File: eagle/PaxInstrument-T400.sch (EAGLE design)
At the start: 115 parts, among them IC1 MCP3424, J1 MICRO-SDCARD-CONNECTOR-330006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, U1 MCP9800, U3 MCP73831, U4 MIC5219-3.3V, U8 NC7S32, X1 FH12-12S-0.5SH, Y1 RESONATORSMD

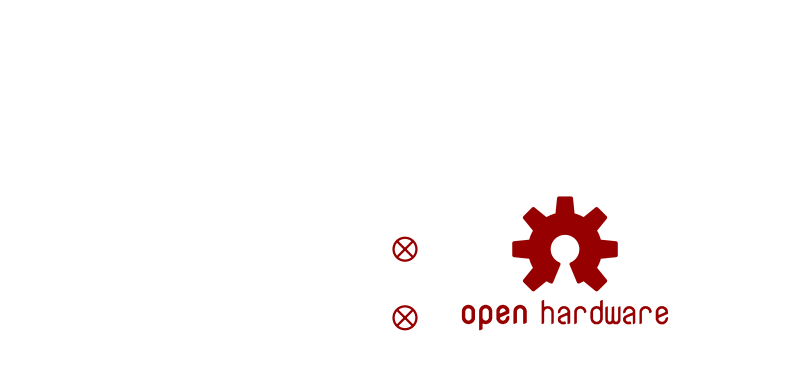
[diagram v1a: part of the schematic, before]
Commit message: Remove fiducials for Rev 0.10
Fix issue Remove fiducials #125
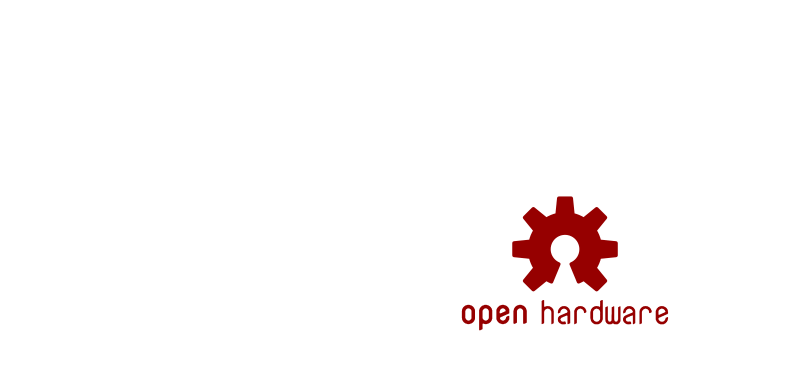
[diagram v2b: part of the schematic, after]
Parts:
- removed FID1, FID2: FIDUCIAL1X2, SparkFun-Aesthetics:FIDUCIAL1X2
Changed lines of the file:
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@@
 <attribute name="OC_DIGIKEY" value="1276-5086-2-ND"/>
-</part>
-<part name="FID1" library="SparkFun-Aesthetics" deviceset="FIDUCIAL" device="1X2">
-<attribute name="MPN" value="N/A"/>
-<attribute name="OC_DIGIKEY" value="N/A"/>
-</part>
-<part name="FID2" library="SparkFun-Aesthetics" deviceset="FIDUCIAL" device="1X2">
-<attribute name="MPN" value="N/A"/>
-<attribute name="OC_DIGIKEY" value="N/A"/>
 </part>
 <part name="U$1" library="blinkinlabs" deviceset="USB_MICRO" device="SMT+THRUHULE">
@@
 <attribute name="MPN" x="124.46" y="200.66" size="1.778" layer="96" display="off"/>
 </instance>
-<instance part="FID1" gate="G$1" x="254" y="15.24">
-<attribute name="MPN" x="254" y="15.24" size="1.778" layer="96" display="off"/>
-<attribute name="OC_DIGIKEY" x="254" y="15.24" size="1.778" layer="96" display="off"/>
-</instance>
-<instance part="FID2" gate="G$1" x="254" y="7.62">
-<attribute name="MPN" x="254" y="7.62" size="1.778" layer="96" display="off"/>
-<attribute name="OC_DIGIKEY" x="254" y="7.62" size="1.778" layer="96" display="off"/>
-</instance>
 <instance part="U$1" gate="G$1" x="17.78" y="233.68">

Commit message: Changed Longer soler pads on 2x3 header footprint for Rev 0.10
Changed Longer soler pads on 2x3 header footprint #122
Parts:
- ICSP, ICSP1: device SparkFun-Connectors:M03X2SMT -> PaxInstrument-T400:SPARKFUN-CONNECTORS_M03X2PAX
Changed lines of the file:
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@@
 <grid distance="0.1" unitdist="inch" unit="inch" style="lines" multiple="1" display="no" altdistance="0.01" altunitdist="inch" altunit="inch"/>
 <layers>
-<layer number="1" name="Top" color="4" fill="1" visible="no" active="no"/>
-<layer number="2" name="Route2" color="1" fill="3" visible="no" active="no"/>
-<layer number="3" name="Route3" color="4" fill="3" visible="no" active="no"/>
-<layer number="4" name="Route4" color="1" fill="4" visible="no" active="no"/>
-<layer number="5" name="Route5" color="4" fill="4" visible="no" active="no"/>
-<layer number="6" name="Route6" color="1" fill="8" visible="no" active="no"/>
-<layer number="7" name="Route7" color="4" fill="8" visible="no" active="no"/>
-<layer number="8" name="Route8" color="1" fill="2" visible="no" active="no"/>
-<layer number="9" name="Route9" color="4" fill="2" visible="no" active="no"/>
-<layer number="10" name="Route10" color="1" fill="7" visible="no" active="no"/>
-<layer number="11" name="Route11" color="4" fill="7" visible="no" active="no"/>
-<layer number="12" name="Route12" color="1" fill="5" visible="no" active="no"/>
-<layer number="13" name="Route13" color="4" fill="5" visible="no" active="no"/>
-<layer number="14" name="Route14" color="1" fill="6" visible="no" active="no"/>
-<layer number="15" name="Route15" color="4" fill="6" visible="no" active="no"/>
-<layer number="16" name="Bottom" color="1" fill="1" visible="no" active="no"/>
-<layer number="17" name="Pads" color="2" fill="1" visible="no" active="no"/>
-<layer number="18" name="Vias" color="2" fill="1" visible="no" active="no"/>
-<layer number="19" name="Unrouted" color="6" fill="1" visible="no" active="no"/>
-<layer number="20" name="Dimension" color="13" fill="1" visible="no" active="no"/>
-<layer number="21" name="tPlace" color="7" fill="1" visible="no" active="no"/>
-<layer number="22" name="bPlace" color="14" fill="1" visible="no" active="no"/>
-<layer number="23" name="tOrigins" color="15" fill="1" visible="no" active="no"/>
-<layer number="24" name="bOrigins" color="15" fill="1" visible="no" active="no"/>
-<layer number="25" name="tNames" color="7" fill="1" visible="no" active="no"/>
-<layer number="26" name="bNames" color="7" fill="1" visible="no" active="no"/>
-<layer number="27" name="tValues" color="7" fill="1" visible="no" active="no"/>
-<layer number="28" name="bValues" color="7" fill="1" visible="no" active="no"/>
+<layer number="1" name="Top" color="4" fill="1" visible="yes" active="no"/>
+<layer number="2" name="Route2" color="1" fill="3" visible="yes" active="no"/>
+<layer number="3" name="Route3" color="4" fill="3" visible="yes" active="no"/>
+<layer number="4" name="Route4" color="1" fill="4" visible="yes" active="no"/>
+<layer number="5" name="Route5" color="4" fill="4" visible="yes" active="no"/>
+<layer number="6" name="Route6" color="1" fill="8" visible="yes" active="no"/>
+<layer number="7" name="Route7" color="4" fill="8" visible="yes" active="no"/>
+<layer number="8" name="Route8" color="1" fill="2" visible="yes" active="no"/>
+<layer number="9" name="Route9" color="4" fill="2" visible="yes" active="no"/>
+<layer number="10" name="Route10" color="1" fill="7" visible="yes" active="no"/>
+<layer number="11" name="Route11" color="4" fill="7" visible="yes" active="no"/>
+<layer number="12" name="Route12" color="1" fill="5" visible="yes" active="no"/>
+<layer number="13" name="Route13" color="4" fill="5" visible="yes" active="no"/>
+<layer number="14" name="Route14" color="1" fill="6" visible="yes" active="no"/>
+<layer number="15" name="Route15" color="4" fill="6" visible="yes" active="no"/>
+<layer number="16" name="Bottom" color="1" fill="1" visible="yes" active="no"/>
+<layer number="17" name="Pads" color="2" fill="1" visible="yes" active="no"/>
+<layer number="18" name="Vias" color="2" fill="1" visible="yes" active="no"/>
+<layer number="19" name="Unrouted" color="6" fill="1" visible="yes" active="no"/>
+<layer number="20" name="Dimension" color="13" fill="1" visible="yes" active="no"/>
+<layer number="21" name="tPlace" color="7" fill="1" visible="yes" active="no"/>
+<layer number="22" name="bPlace" color="14" fill="1" visible="yes" active="no"/>
+<layer number="23" name="tOrigins" color="15" fill="1" visible="yes" active="no"/>
+<layer number="24" name="bOrigins" color="15" fill="1" visible="yes" active="no"/>
+<layer number="25" name="tNames" color="7" fill="1" visible="yes" active="no"/>
+<layer number="26" name="bNames" color="7" fill="1" visible="yes" active="no"/>
+<layer number="27" name="tValues" color="7" fill="1" visible="yes" active="no"/>
+<layer number="28" name="bValues" color="7" fill="1" visible="yes" active="no"/>
 <layer number="29" name="tStop" color="7" fill="3" visible="no" active="no"/>
 <layer number="30" name="bStop" color="7" fill="6" visible="no" active="no"/>
@@
 <layer number="35" name="tGlue" color="7" fill="4" visible="no" active="no"/>
 <layer number="36" name="bGlue" color="7" fill="5" visible="no" active="no"/>
-<layer number="37" name="tTest" color="7" fill="1" visible="no" active="no"/>
-<layer number="38" name="bTest" color="7" fill="1" visible="no" active="no"/>
+<layer number="37" name="tTest" color="7" fill="1" visible="yes" active="no"/>
+<layer number="38" name="bTest" color="7" fill="1" visible="yes" active="no"/>
 <layer number="39" name="tKeepout" color="4" fill="11" visible="no" active="no"/>
 <layer number="40" name="bKeepout" color="1" fill="11" visible="no" active="no"/>
@@
 <layer number="44" name="Drills" color="7" fill="1" visible="no" active="no"/>
 <layer number="45" name="Holes" color="7" fill="1" visible="no" active="no"/>
-<layer number="46" name="Milling" color="3" fill="1" visible="no" active="no"/>
-<layer number="47" name="Measures" color="7" fill="1" visible="no" active="no"/>
-<layer number="48" name="Document" color="7" fill="1" visible="no" active="no"/>
-<layer number="49" name="Reference" color="7" fill="1" visible="no" active="no"/>
-<layer number="50" name="dxf" color="7" fill="1" visible="no" active="no"/>
-<layer number="51" name="tDocu" color="6" fill="1" visible="no" active="no"/>
-<layer number="52" name="bDocu" color="7" fill="1" visible="no" active="no"/>
-<layer number="53" name="tGND_GNDA" color="7" fill="9" visible="no" active="no"/>
-<layer number="54" name="bGND_GNDA" color="1" fill="9" visible="no" active="no"/>
-<layer number="56" name="wert" color="7" fill="1" visible="no" active="no"/>
+<layer number="46" name="Milling" color="3" fill="1" visible="yes" active="no"/>
+<layer number="47" name="Measures" color="7" fill="1" visible="yes" active="no"/>
+<layer number="48" name="Document" color="7" fill="1" visible="yes" active="no"/>
+<layer number="49" name="Reference" color="7" fill="1" visible="yes" active="no"/>
+<layer number="50" name="dxf" color="7" fill="1" visible="yes" active="no"/>
+<layer number="51" name="tDocu" color="6" fill="1" visible="yes" active="no"/>
+<layer number="52" name="bDocu" color="7" fill="1" visible="yes" active="no"/>
+<layer number="53" name="tGND_GNDA" color="7" fill="9" visible="yes" active="no"/>
+<layer number="54" name="bGND_GNDA" color="1" fill="9" visible="yes" active="no"/>
+<layer number="56" name="wert" color="7" fill="1" visible="yes" active="no"/>
 <layer number="91" name="Nets" color="2" fill="1" visible="yes" active="yes"/>
 <layer number="92" name="Busses" color="1" fill="1" visible="yes" active="yes"/>
@@
 <parts>
 <part name="FRAME1" library="SparkFun" deviceset="FRAME-A3" device=""/>
-<part name="ICSP" library="SparkFun-Connectors" deviceset="M03X2" device="SMT" value="ICSP">
+<part name="ICSP" library="PaxInstrument-T400" deviceset="SPARKFUN-CONNECTORS_M03X2" device="PAX" value="ICSP">
 <attribute name="MPN" value="95278-101A06LF"/>
 <attribute name="OC_DIGIKEY" value="609-3487-2-ND"/>
@@
 <attribute name="OC_DIGIKEY" value="1276-5086-2-ND"/>
 </part>
-<part name="ICSP1" library="SparkFun-Connectors" deviceset="M03X2" device="SMT" value="ICSP">
+<part name="ICSP1" library="PaxInstrument-T400" deviceset="SPARKFUN-CONNECTORS_M03X2" device="PAX" value="ICSP">
 <attribute name="MPN" value="95278-101A06LF"/>
 <attribute name="OC_DIGIKEY" value="609-3487-2-ND"/>

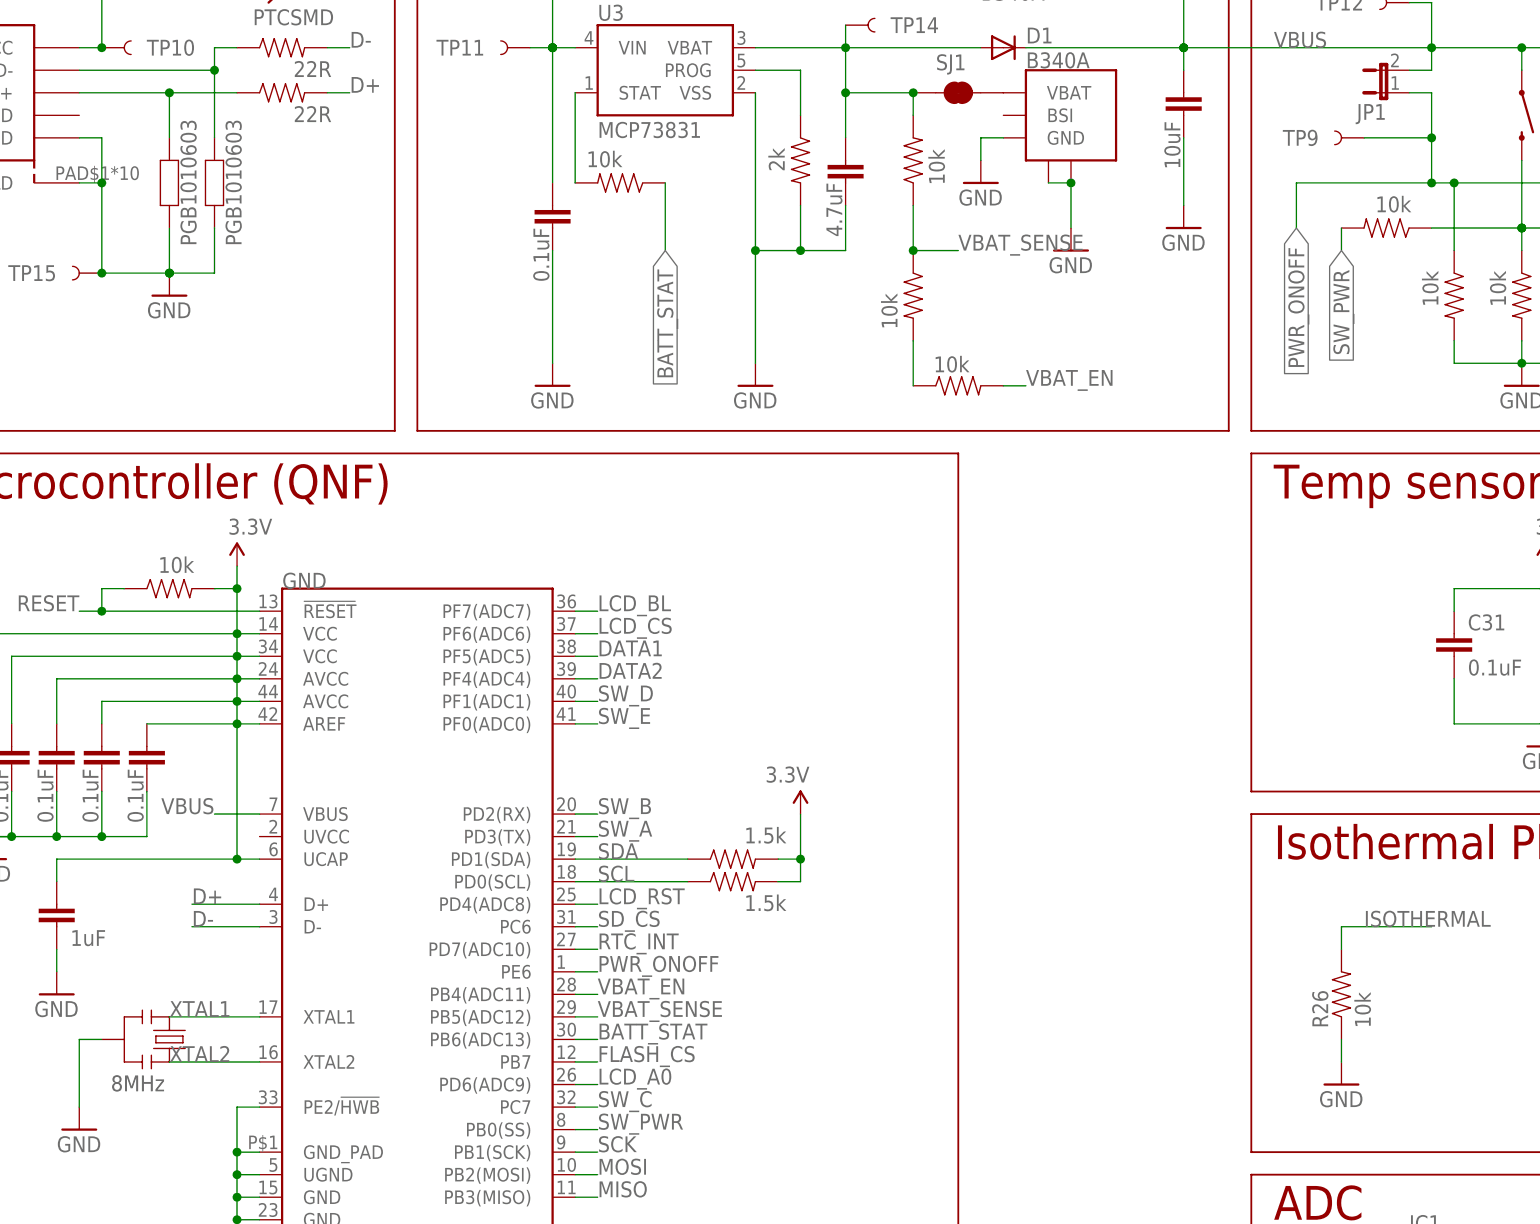
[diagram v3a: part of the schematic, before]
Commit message: Switch to 0603
Switch to 0603 #121
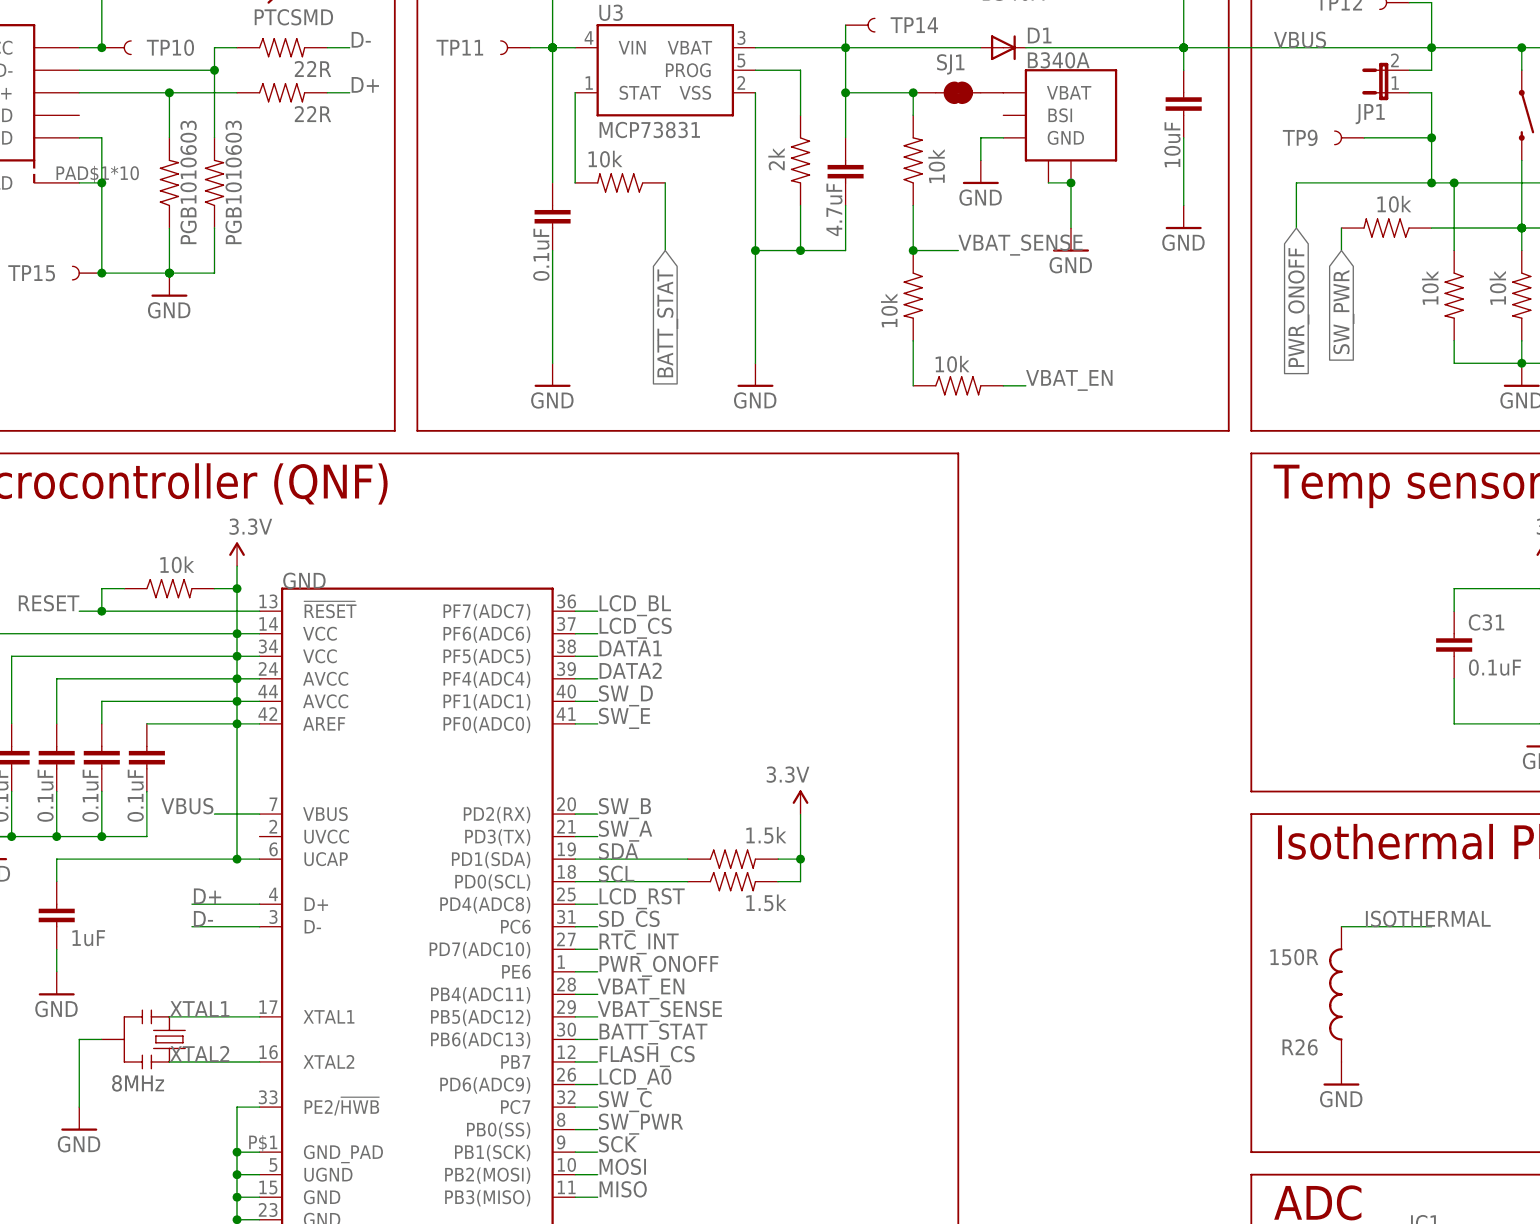
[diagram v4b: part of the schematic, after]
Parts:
- C1, C10, C11, C13, C14, C15, C16, C17, C18, C19, C2, C20, C24, C25, C27, C28, C29, C3, C30, C31, C32, C33, C34, C35, C36, C37, C4, C5, C6, C7, C8, C9: device SparkFun-Passives:CAP0805 -> PaxInstrument-T400:SPARKFUN-CAPACITORS_CAP0603-CAP
- C12, C26: device SparkFun-Passives:CAP0805 -> PaxInstrument-T400:SPARKFUN-CAPACITORS_CAP0805
- R1, R10, R11, R12, R13, R14, R15, R16, R17, R19, R2, R20, R24, R25, R27, R28, R29, R3, R30, R31, R32, R33, R34, R35, R36, R37, R38, R39, R4, R40, R41, R42, R6, R7, R8, R9: device SparkFun-Passives:RESISTOR0805-RES -> PaxInstrument-T400:SPARKFUN-RESISTORS_RESISTOR0603-RES
- R26: value 10k -> 150R; device SparkFun-Passives:RESISTOR0805-RES -> PaxInstrument-T400:INDUCTOR30OHM,1.8A
- Z1, Z2: device freetronics-master-v1.1:RESISTOR0603 -> PaxInstrument-T400:SPARKFUN-RESISTORS_RESISTOR0603-RES
